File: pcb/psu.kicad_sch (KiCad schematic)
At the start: 7 parts, among them U1 LM78L05_SO8

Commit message: Tweak PSU
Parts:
- removed C2: C, symbol Device:C
- removed D1: RECTIFIER, symbol Device:D_Bridge_+-AA
- removed RV1, RV2: Varistor, symbol Device:Varistor
- added C27: 100u, symbol Device:C_Polarized_US
- added D10, D11, D12, D9: SB2060, symbol Device:D_Schottky
- F1: value Fuse -> 5A
- renumbered C1 to C26, U1 to U8
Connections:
- net AC_N: now also D10.1 (K), D12.2 (A)
- net GND: now also C27.2, D10.2 (A), D9.2 (A)
- net VCC: now also C27.1
- net Vdrive: now also D11.1 (K), D12.1 (K)
- net at F1.1: now also D11.2 (A), D9.1 (K)
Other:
- note added: "AC stepped down and isolated by external PSU board to 20VAC."
- note added: "Need a choke in series with C26 to limit in-rush?"
- note added: "These don't need to be Schottkys, but these are the cheapest and we get a lower forward voltage, so might as well."
- note removed: "AC stepped down by external PSU board to 20VAC."
- note removed: "Need a choke in series with CP1 to limit in-rush?"
- title: (none) -> Power Supply
- moved on the sheet: F1

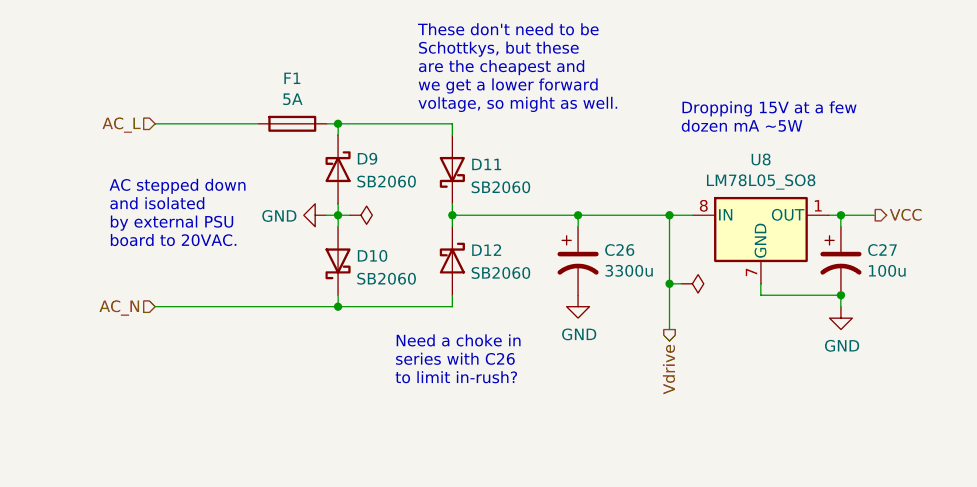
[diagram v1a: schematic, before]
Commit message: Add MOV to protect full bridge
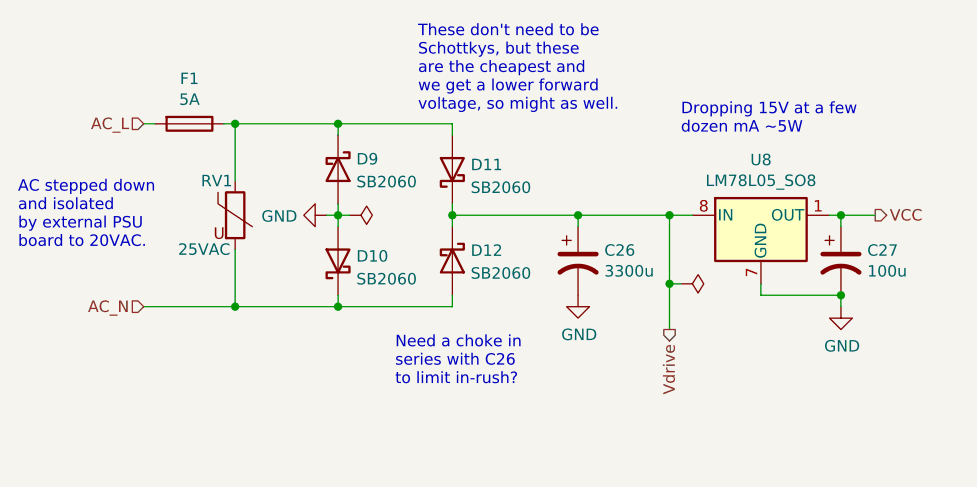
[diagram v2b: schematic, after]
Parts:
- added RV1: 25VAC, symbol Device:Varistor
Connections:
- net AC_N: now also RV1.2
- net at D11.2 (A), D9.1 (K), F1.1: now also RV1.1
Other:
- moved on the sheet: F1
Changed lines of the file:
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@@
     (company "Zach Anderson")
   )
+  (junction (at 114.3 99.06) (diameter 0) (color 0 0 0 0)
+  )
   (junction (at 125.73 78.74) (diameter 0) (color 0 0 0 0)
   )
@@
   (junction (at 181.61 97.79) (diameter 0) (color 0 0 0 0)
   )
+  (junction (at 114.3 78.74) (diameter 0) (color 0 0 0 0)
+  )
   (wire (pts (xy 152.4 88.9) (xy 162.56 88.9))
     (stroke (width 0) (type default) (color 0 0 0 0))
@@
     (stroke (width 0) (type default) (color 0 0 0 0))
   )
+  (wire (pts (xy 114.3 78.74) (xy 125.73 78.74))
+    (stroke (width 0) (type default) (color 0 0 0 0))
+  )
   (wire (pts (xy 125.73 88.9) (xy 125.73 90.17))
     (stroke (width 0) (type default) (color 0 0 0 0))
@@
     (stroke (width 0) (type default) (color 0 0 0 0))
   )
-  (wire (pts (xy 105.41 78.74) (xy 116.84 78.74))
+  (wire (pts (xy 104.14 78.74) (xy 105.41 78.74))
     (stroke (width 0) (type default) (color 0 0 0 0))
   )
@@
     (stroke (width 0) (type default) (color 0 0 0 0))
   )
-  (wire (pts (xy 124.46 78.74) (xy 125.73 78.74))
-    (stroke (width 0) (type default) (color 0 0 0 0))
-  )
-  (wire (pts (xy 105.41 99.06) (xy 125.73 99.06))
+  (wire (pts (xy 113.03 78.74) (xy 114.3 78.74))
+    (stroke (width 0) (type default) (color 0 0 0 0))
+  )
+  (wire (pts (xy 114.3 78.74) (xy 114.3 85.09))
+    (stroke (width 0) (type default) (color 0 0 0 0))
+  )
+  (wire (pts (xy 104.14 99.06) (xy 114.3 99.06))
+    (stroke (width 0) (type default) (color 0 0 0 0))
+  )
+  (wire (pts (xy 114.3 92.71) (xy 114.3 99.06))
     (stroke (width 0) (type default) (color 0 0 0 0))
   )
@@
   )
   (wire (pts (xy 162.56 88.9) (xy 165.1 88.9))
+    (stroke (width 0) (type default) (color 0 0 0 0))
+  )
+  (wire (pts (xy 114.3 99.06) (xy 125.73 99.06))
     (stroke (width 0) (type default) (color 0 0 0 0))
   )
@@
   )
   (text "AC stepped down\nand isolated\nby external PSU\nboard to 20VAC."
-    (at 100.33 92.71 0)
+    (at 90.17 92.71 0)
     (effects (font (size 1.27 1.27)) (justify left bottom))
   )
-  (hierarchical_label "AC_N" (shape input) (at 105.41 99.06 180)
+  (hierarchical_label "AC_N" (shape input) (at 104.14 99.06 180)
     (effects (font (size 1.27 1.27)) (justify right))
   )
@@
     (effects (font (size 1.27 1.27)) (justify left))
   )
-  (hierarchical_label "AC_L" (shape input) (at 105.41 78.74 180)
+  (hierarchical_label "AC_L" (shape input) (at 104.14 78.74 180)
     (effects (font (size 1.27 1.27)) (justify right))
   )
-  (symbol (lib_id "Device:Fuse") (at 120.65 78.74 270) (unit 1)
-    (in_bom yes) (on_board yes)
-    (property "Reference" "F1" (id 0) (at 120.65 73.7362 90))
-    (property "Value" "5A" (id 1) (at 120.65 76.0476 90))
-    (property "Footprint" "" (id 2) (at 120.65 76.962 90)
-      (effects (font (size 1.27 1.27)) hide)
-    )
-    (property "Datasheet" "~" (id 3) (at 120.65 78.74 0)
+  (symbol (lib_id "Device:Fuse") (at 109.22 78.74 270) (unit 1)
+    (in_bom yes) (on_board yes)
+    (property "Reference" "F1" (id 0) (at 109.22 73.7362 90))
+    (property "Value" "5A" (id 1) (at 109.22 76.0476 90))
+    (property "Footprint" "" (id 2) (at 109.22 76.962 90)
+      (effects (font (size 1.27 1.27)) hide)
+    )
+    (property "Datasheet" "~" (id 3) (at 109.22 78.74 0)
       (effects (font (size 1.27 1.27)) hide)
     )
@@
       (effects (font (size 1.27 1.27)) hide)
     )
+    (pin "1")
+    (pin "2")
+  )
+  (symbol (lib_id "Device:Varistor") (at 114.3 88.9 0) (unit 1)
+    (in_bom yes) (on_board yes)
+    (property "Reference" "RV1" (id 0) (at 110.49 85.09 0)
+      (effects (font (size 1.27 1.27)) (justify left))
+    )
+    (property "Value" "25VAC" (id 1) (at 107.95 92.71 0)
+      (effects (font (size 1.27 1.27)) (justify left))
+    )
+    (property "Footprint" "" (id 2) (at 112.522 88.9 90)
+      (effects (font (size 1.27 1.27)) hide)
+    )
+    (property "Datasheet" "https://datasheets.kyocera-avx.com/autotguard.pdf" (id 3) (at 114.3 88.9 0)
+      (effects (font (size 1.27 1.27)) hide)
+    )
